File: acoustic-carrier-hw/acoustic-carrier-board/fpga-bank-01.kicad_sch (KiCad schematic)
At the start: 0 parts

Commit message: [carrier] Added hierarchical labels
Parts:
- added C28, C29: 0.1uF, Capacitor_SMD:C_0402_1005Metric, symbol Device:C_Small
- added C30: 10uF, Capacitor_SMD:C_0603_1608Metric, symbol Device:C_Small
- added C31: 10nF, Capacitor_SMD:C_0402_1005Metric, symbol Device:C_Small
- added IC1: ECP5-BGA256, iw-fpga_mcu:BGA256C80P16X16_1400X1400X170, symbol iw-fpga_mcu:ECP5-BGA256
- added R3: 0, Resistor_SMD:R_0603_1608Metric, symbol Device:R_Small
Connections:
- new net: IC1.D9 (PT40A), R3.1
- new net B40_EN: IC1.B7 (PT27B/PCLKC0_1)
- new net CLK: IC1.A14 (PT65B), IC1.A15 (PT67B), IC1.A2 (PT4A), IC1.E12 (PT58B)
- new net CTL: IC1.A11 (PT53A), IC1.B13 (PT60A)
- new net D0: IC1.A12 (PT53B), IC1.B3 (PT4B), IC1.C13 (PT60B)
- new net D1: IC1.A3 (PT6A), IC1.B12 (PT56A), IC1.D13 (PT62A)
- new net D2: IC1.A4 (PT6B), IC1.C12 (PT56B), IC1.E13 (PT62B)
- new net D3: IC1.A13 (PT65A), IC1.D12 (PT58A), IC1.E4 (PT9A)
- new net D4: IC1.D4 (PT9B)
- new net D5: IC1.C4 (PT11A)
- new net D6: IC1.B4 (PT11B)
- new net D7: IC1.E5 (PT13A)
- new net D8: IC1.D5 (PT13B)
- new net D9: IC1.C5 (PT15A)
- new net DATA: IC1.B14 (PT67A)
- new net ETH_REFCLK: IC1.C9 (PT38B/GR_PCLK1_1)
- new net FPGA_ADC_LED0: IC1.A6 (PT18B)
- new net FPGA_ADC_LED1: IC1.A5 (PT18A)
- new net FPGA_ADC_SW: IC1.E6 (PT20A)
- new net GND: C28.2, C29.2, C30.2, C31.2
- new net OTR: IC1.B5 (PT15B)
- new net PWM0: IC1.C6 (PT22A)
- new net PWM1: IC1.B6 (PT22B)
- new net PWM2: IC1.E7 (PT24A/GR_PCLK0_1)
- new net PWM3: IC1.D7 (PT24B/GR_PCLK0_0)
- new net S10V_EN: IC1.C7 (PT27A/PCLKT0_1)
- new net T_SCL: IC1.A7 (PT29A/PCLKT0_0)
- new net T_SDA: IC1.A8 (PT29B/PCLKC0_0)
- new net VCORE_3V3: C28.1, C29.1, C30.1, C31.1, IC1.F10 (VCCIO1_1), IC1.F11 (VCCIO1_2), IC1.F6 (VCCIO0_1), IC1.F7 (VCCIO0_2)
- new net ~{ETH_INT}: IC1.E9 (PT40B)
- new net ~{ETH_RESET}: R3.2
- no-connect marks 0 -> 16
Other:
- note added: "BANK0: ADC"
- note added: "BANK1: ETHERNET"
- note added: "FPGA BANK"
- note added: "TODO: Check whether ethernet bank should be fed with DVDD_H?"

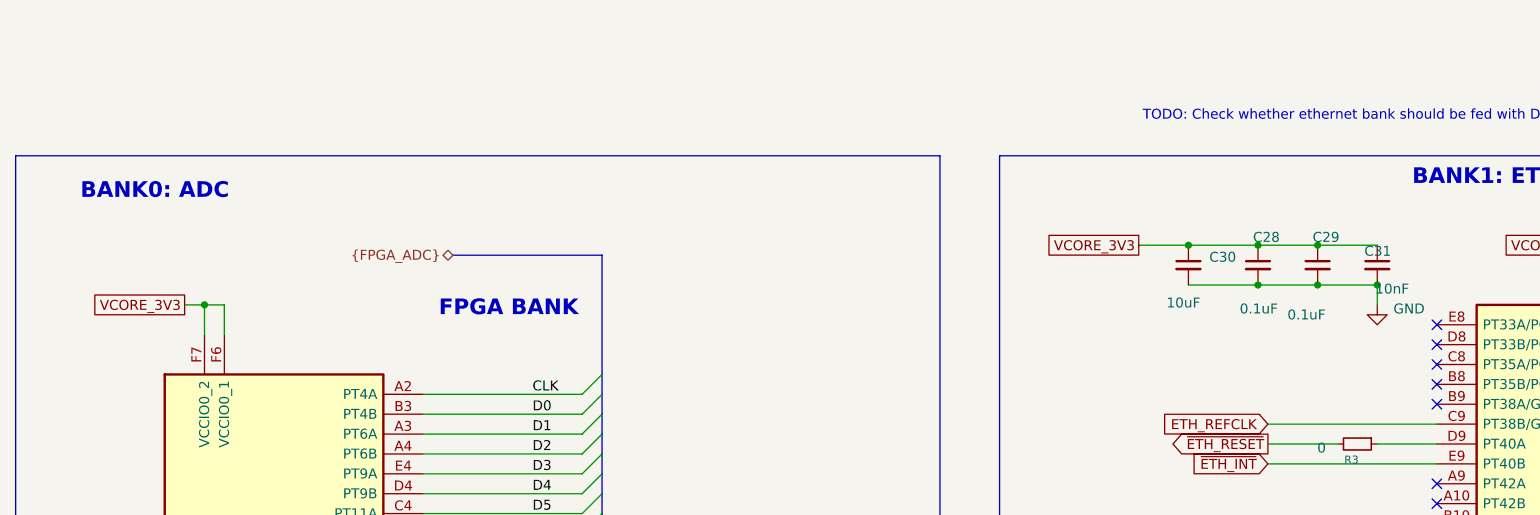
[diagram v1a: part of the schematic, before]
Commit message: [carrier] Added decoupling caps to flash and comparators
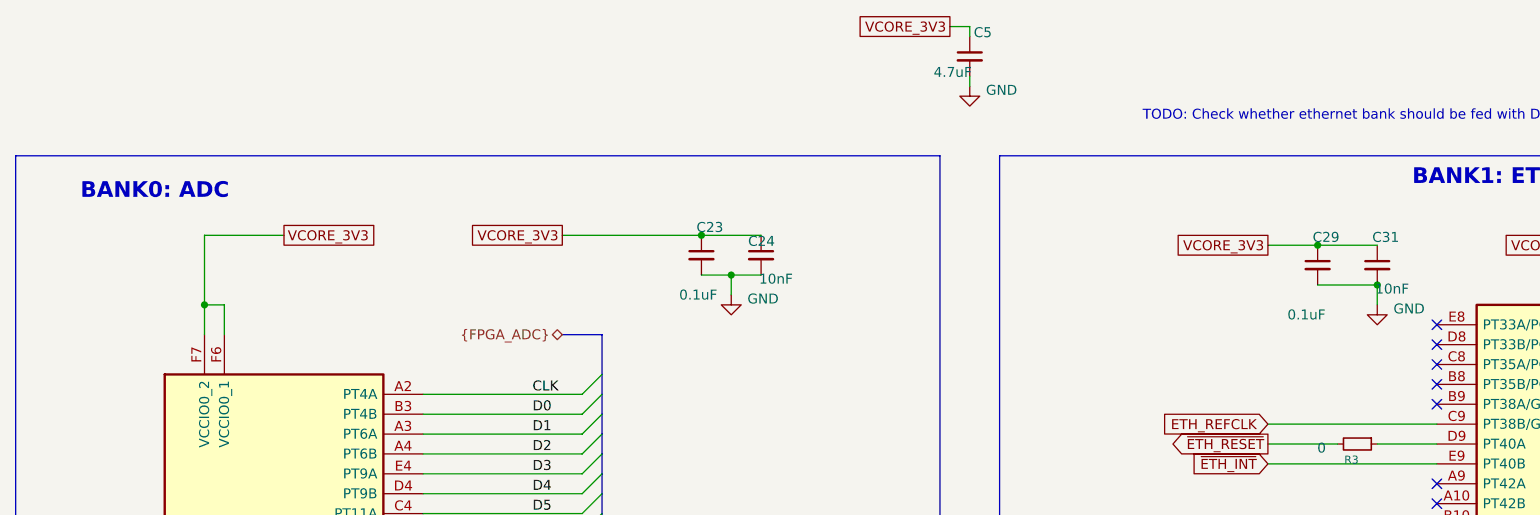
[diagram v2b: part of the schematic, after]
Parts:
- removed C28: 0.1uF, Capacitor_SMD:C_0402_1005Metric, symbol Device:C_Small
- removed C30: 10uF, Capacitor_SMD:C_0603_1608Metric, symbol Device:C_Small
- added C23: 0.1uF, Capacitor_SMD:C_0402_1005Metric, symbol Device:C_Small
- added C24: 10nF, Capacitor_SMD:C_0402_1005Metric, symbol Device:C_Small
- added C5: 4.7uF, Capacitor_SMD:C_0402_1005Metric, symbol Device:C_Small
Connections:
- net GND: now also C23.2, C24.2, C5.2
- net VCORE_3V3: now also C23.1, C24.1, C5.1
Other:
- note removed: "FPGA BANK"

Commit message: [carrier] Added extra decoupling to ECP5U according to datasheet (next) perform page-wise checks, add testpoints
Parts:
- removed C31: 10nF, Capacitor_SMD:C_0402_1005Metric, symbol Device:C_Small
- added C55, C56: 0.1uF, Capacitor_SMD:C_0402_1005Metric, symbol Device:C_Small
- added C58: 4.7uF, Capacitor_SMD:C_0402_1005Metric, symbol Device:C_Small
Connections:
- net GND: now also C55.2, C56.2, C58.2
- net VCORE_3V3: now also C55.1, C56.1, C58.1
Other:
- moved on the sheet: C29

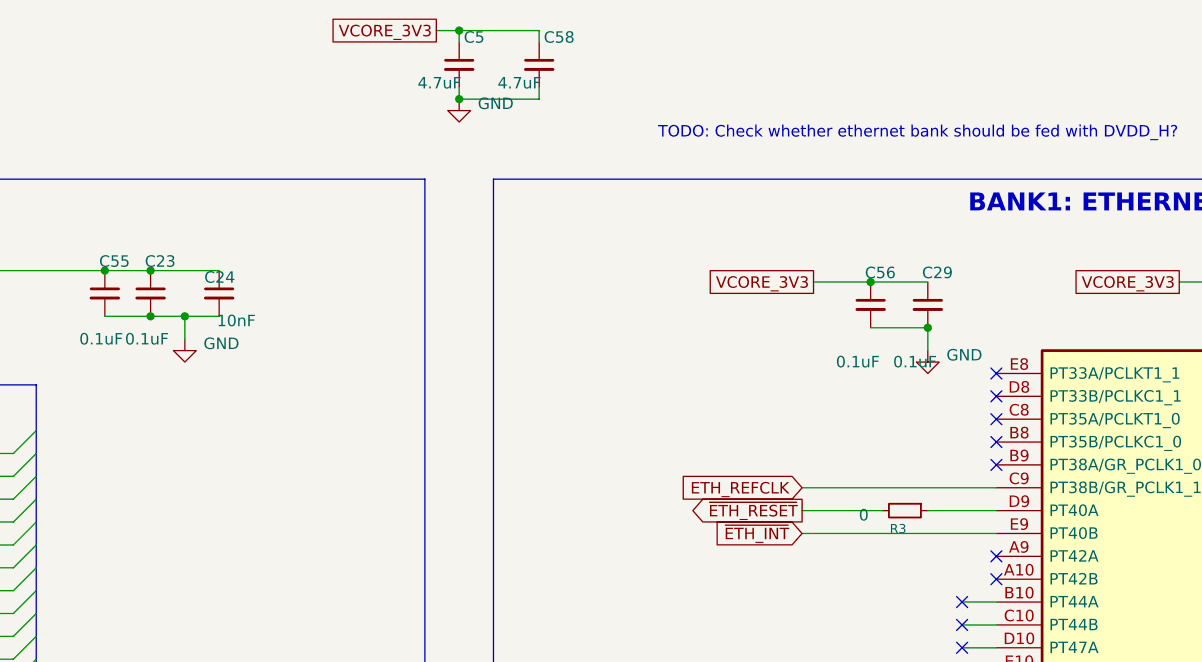
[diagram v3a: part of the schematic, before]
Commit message: [¢arrier] Did major cchecks of ETH, DDR, ANALOG, config (next) check buffer circuit driven by USB-CC, then start layout
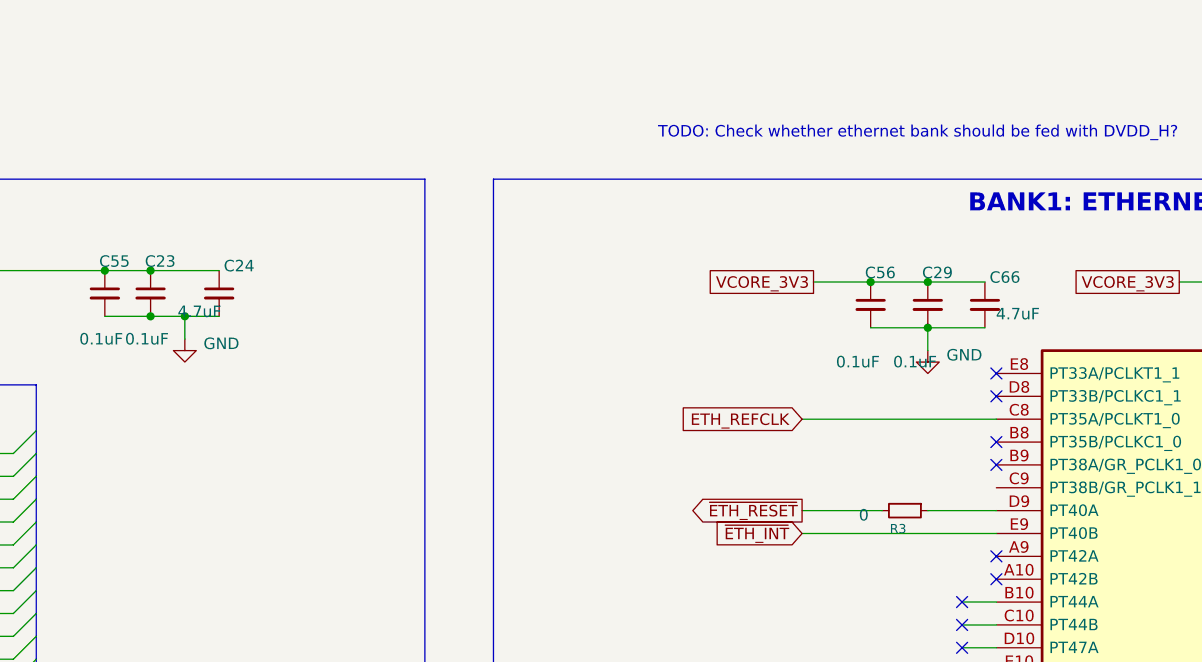
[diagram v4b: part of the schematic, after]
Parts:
- removed C5, C58: 4.7uF, Capacitor_SMD:C_0402_1005Metric, symbol Device:C_Small
- added C66: 4.7uF, Capacitor_SMD:C_0402_1005Metric, symbol Device:C_Small
- C24: value 10nF -> 4.7uF; LPN C15195 -> C23733; MPN CL05B103KB5NNNC -> CL05A475MP5NRNC
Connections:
- net ETH_REFCLK: now also IC1.C8 (PT35A/PCLKT1_0); no longer IC1.C9 (PT38B/GR_PCLK1_1)
- net GND: now also C66.2
- net VCORE_3V3: now also C66.1
- no-connect marks 16 -> 15

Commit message: [¢arrier] Finished checks, startting with layout and routing
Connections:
- net ETH_REFCLK: now also IC1.C9 (PT38B/GR_PCLK1_1); no longer IC1.C8 (PT35A/PCLKT1_0)
- no-connect marks 15 -> 16
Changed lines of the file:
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@@
+	)
+	(no_connect
+		(at 212.09 63.5)
 	)
 	(no_connect
@@
 		)
 	)
+	(wire
+		(pts
+			(xy 198.12 71.12) (xy 212.09 71.12)
+		)
+		(stroke
+			(width 0)
+			(type default)
+		)
+	)
 	(bus
 		(pts
@@
 		(pts
 			(xy 204.47 48.26) (xy 210.82 48.26)
-		)
-		(stroke
-			(width 0)
-			(type default)
-		)
-	)
-	(wire
-		(pts
-			(xy 190.5 63.5) (xy 212.09 63.5)
 		)
 		(stroke
@@
 			)
 			(justify left bottom)
-		)
-	)
-	(global_label "ETH_REFCLK"
-		(shape input)
-		(at 190.5 63.5 180)
-		(fields_autoplaced yes)
-		(effects
-			(font
-				(size 1.27 1.27)
-			)
-			(justify right)
-		)
-		(property "Intersheetrefs" "${INTERSHEET_REFS}"
-			(at 176.0244 63.5 0)
-			(effects
-				(font
-					(size 1.27 1.27)
-				)
-				(justify right)
-				(hide yes)
-			)
 		)
 	)
@@
 			(effects
 				(font
+					(size 1.27 1.27)
+				)
+				(justify right)
+				(hide yes)
+			)
+		)
+	)
+	(global_label "ETH_REFCLK"
+		(shape input)
+		(at 198.12 71.12 180)
+		(fields_autoplaced yes)
+		(effects
+			(font
+				(size 1.27 1.27)
+			)
+			(justify right)
+		)
+		(property "Intersheetrefs" "${INTERSHEET_REFS}"
+			(at 183.6444 71.12 0)
+			(effects
+				(font

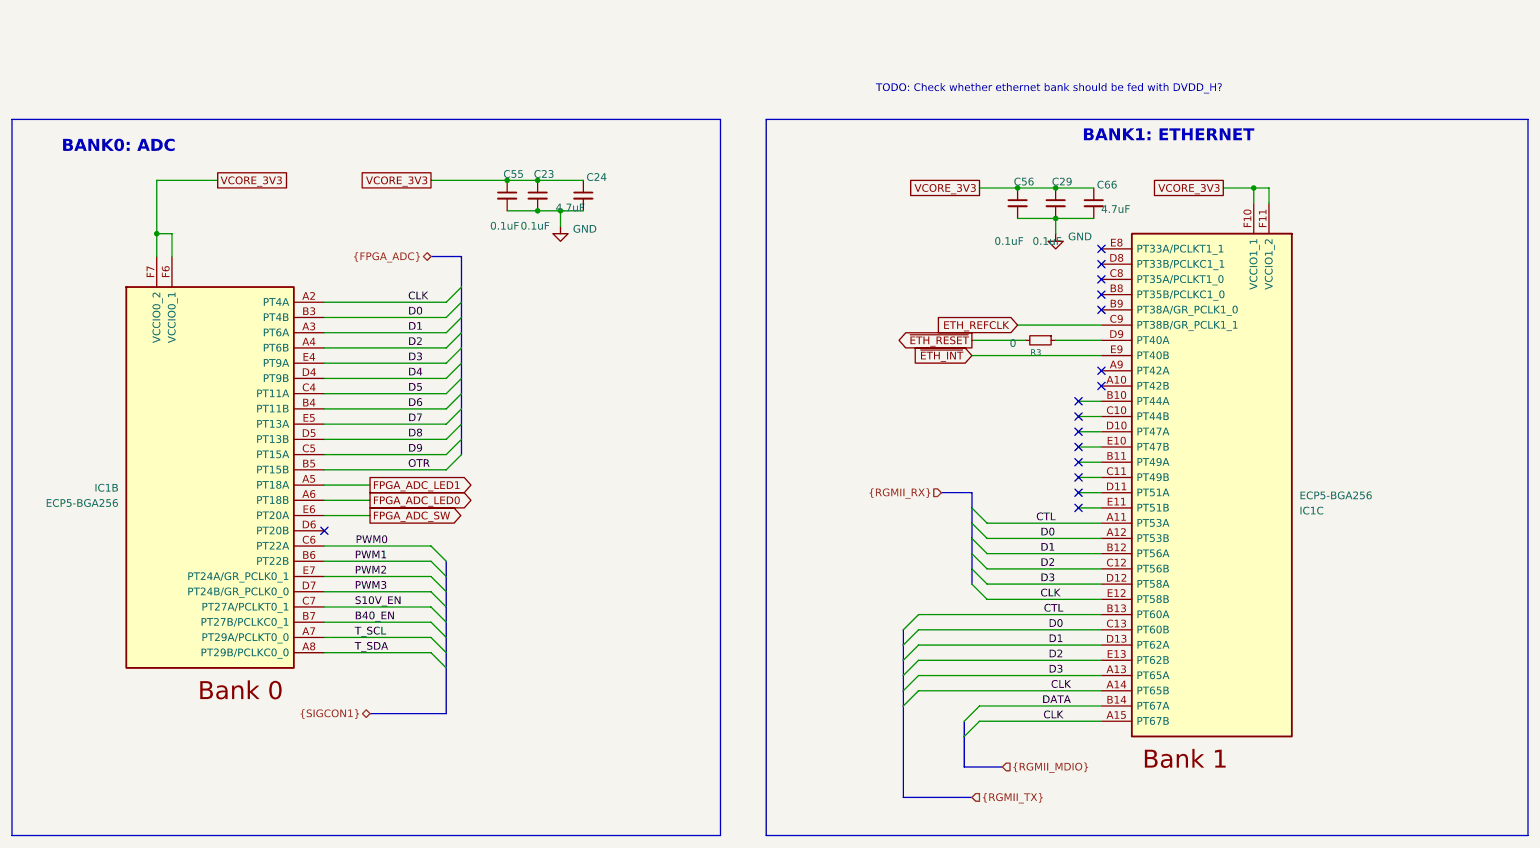
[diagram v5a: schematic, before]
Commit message: [carrier] Added testpoints
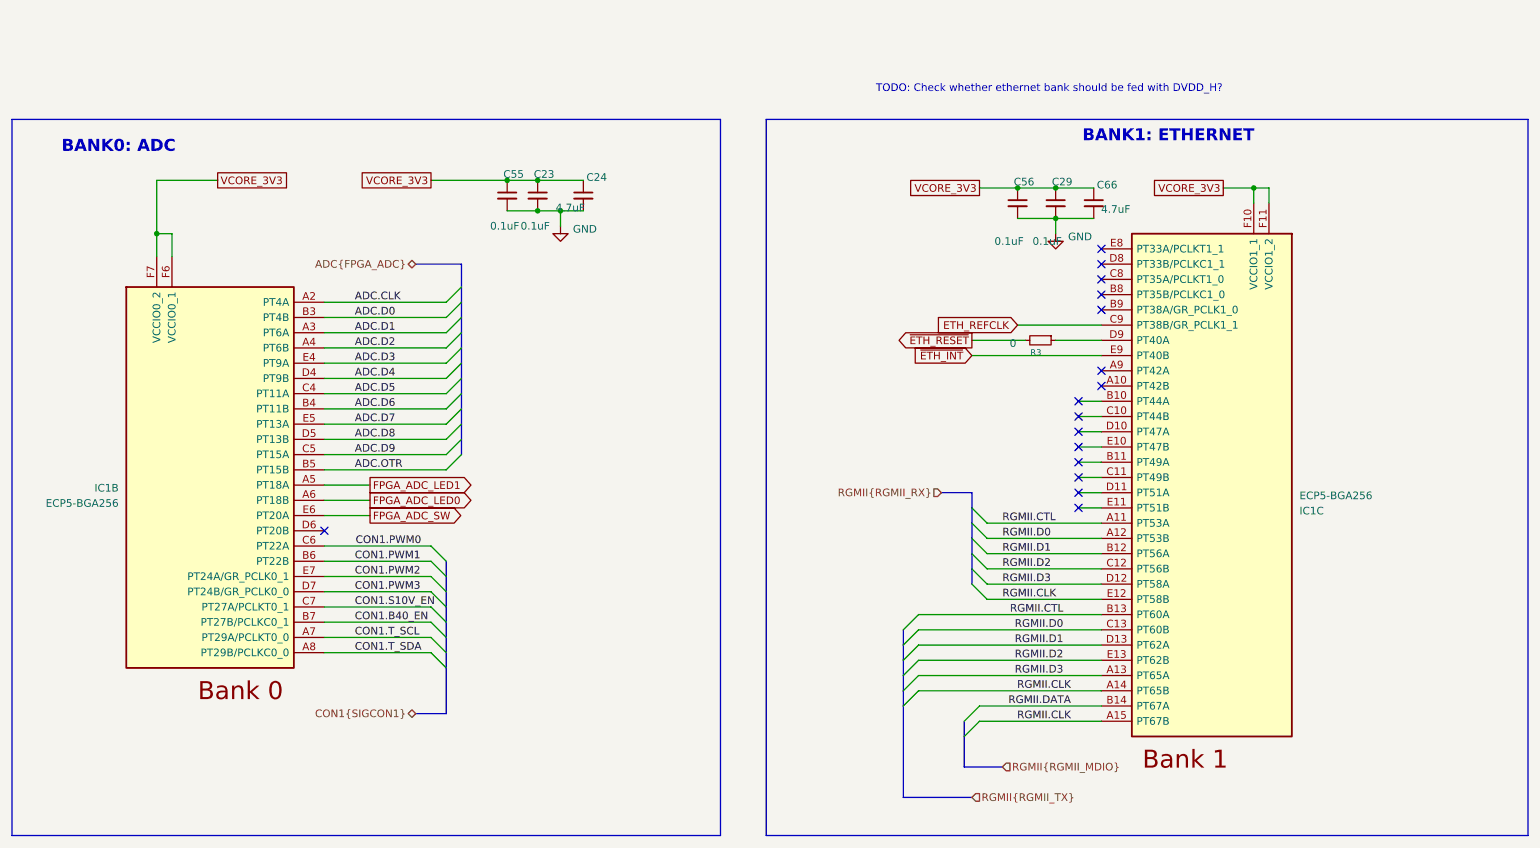
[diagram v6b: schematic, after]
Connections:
- net B40_EN renamed CON1.B40_EN
- net CLK renamed RGMII.CLK
- net RGMII.CLK: no longer IC1.A2 (PT4A)
- net CTL renamed RGMII.CTL
- net D0 renamed RGMII.D0
- net RGMII.D0: no longer IC1.B3 (PT4B)
- net D1 renamed RGMII.D1
- net RGMII.D1: no longer IC1.A3 (PT6A)
- net D2 renamed RGMII.D2
- net RGMII.D2: no longer IC1.A4 (PT6B)
- net D3 renamed RGMII.D3
- net RGMII.D3: no longer IC1.E4 (PT9A)
- net D4 renamed ADC.D4
- net D5 renamed ADC.D5
- net D6 renamed ADC.D6
- net D7 renamed ADC.D7
- net D8 renamed ADC.D8
- net D9 renamed ADC.D9
- net DATA renamed RGMII.DATA
- net OTR renamed ADC.OTR
- net PWM0 renamed CON1.PWM0
- net PWM1 renamed CON1.PWM1
- net PWM2 renamed CON1.PWM2
- net PWM3 renamed CON1.PWM3
- net S10V_EN renamed CON1.S10V_EN
- net T_SCL renamed CON1.T_SCL
- net T_SDA renamed CON1.T_SDA
- new net ADC.CLK: IC1.A2 (PT4A)
- new net ADC.D0: IC1.B3 (PT4B)
- new net ADC.D1: IC1.A3 (PT6A)
- new net ADC.D2: IC1.A4 (PT6B)
- new net ADC.D3: IC1.E4 (PT9A)
